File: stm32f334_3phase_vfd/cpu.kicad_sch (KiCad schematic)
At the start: 16 parts, among them J101 Conn_01x01, J102 Conn_01x01, J103 Conn_01x01, J104 Conn_01x01, U101 STM32F334K6Tx, Y101 Crystal_Small

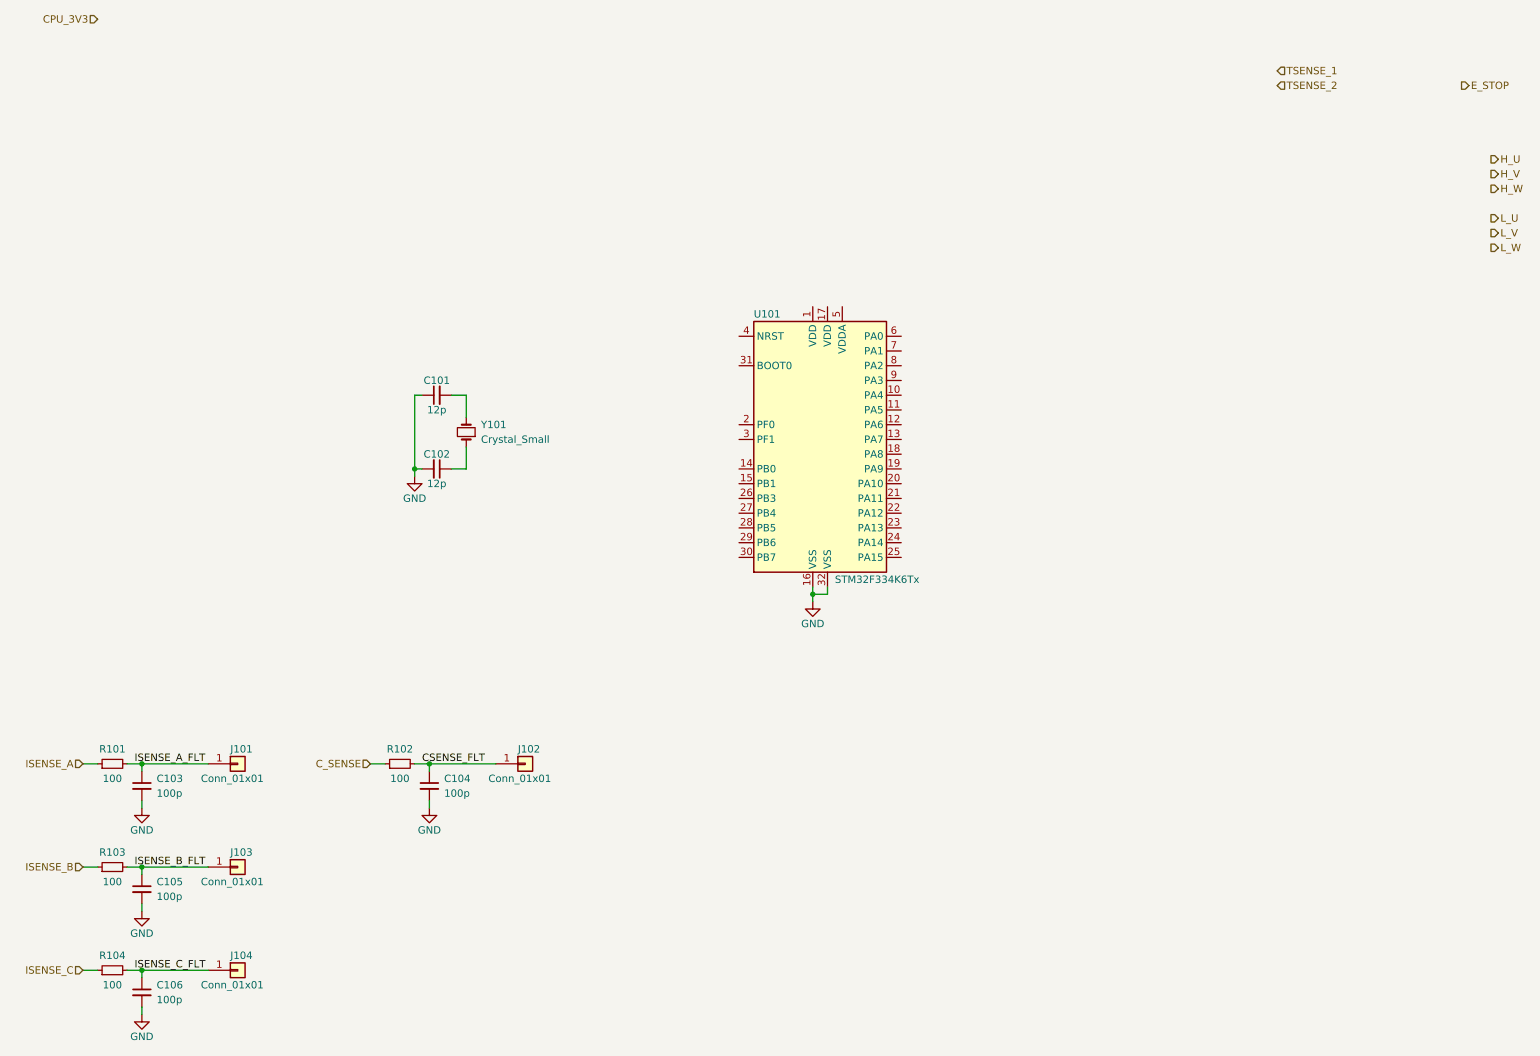
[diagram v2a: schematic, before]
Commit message: switch to LQFP48 cpu, continue workin on layout
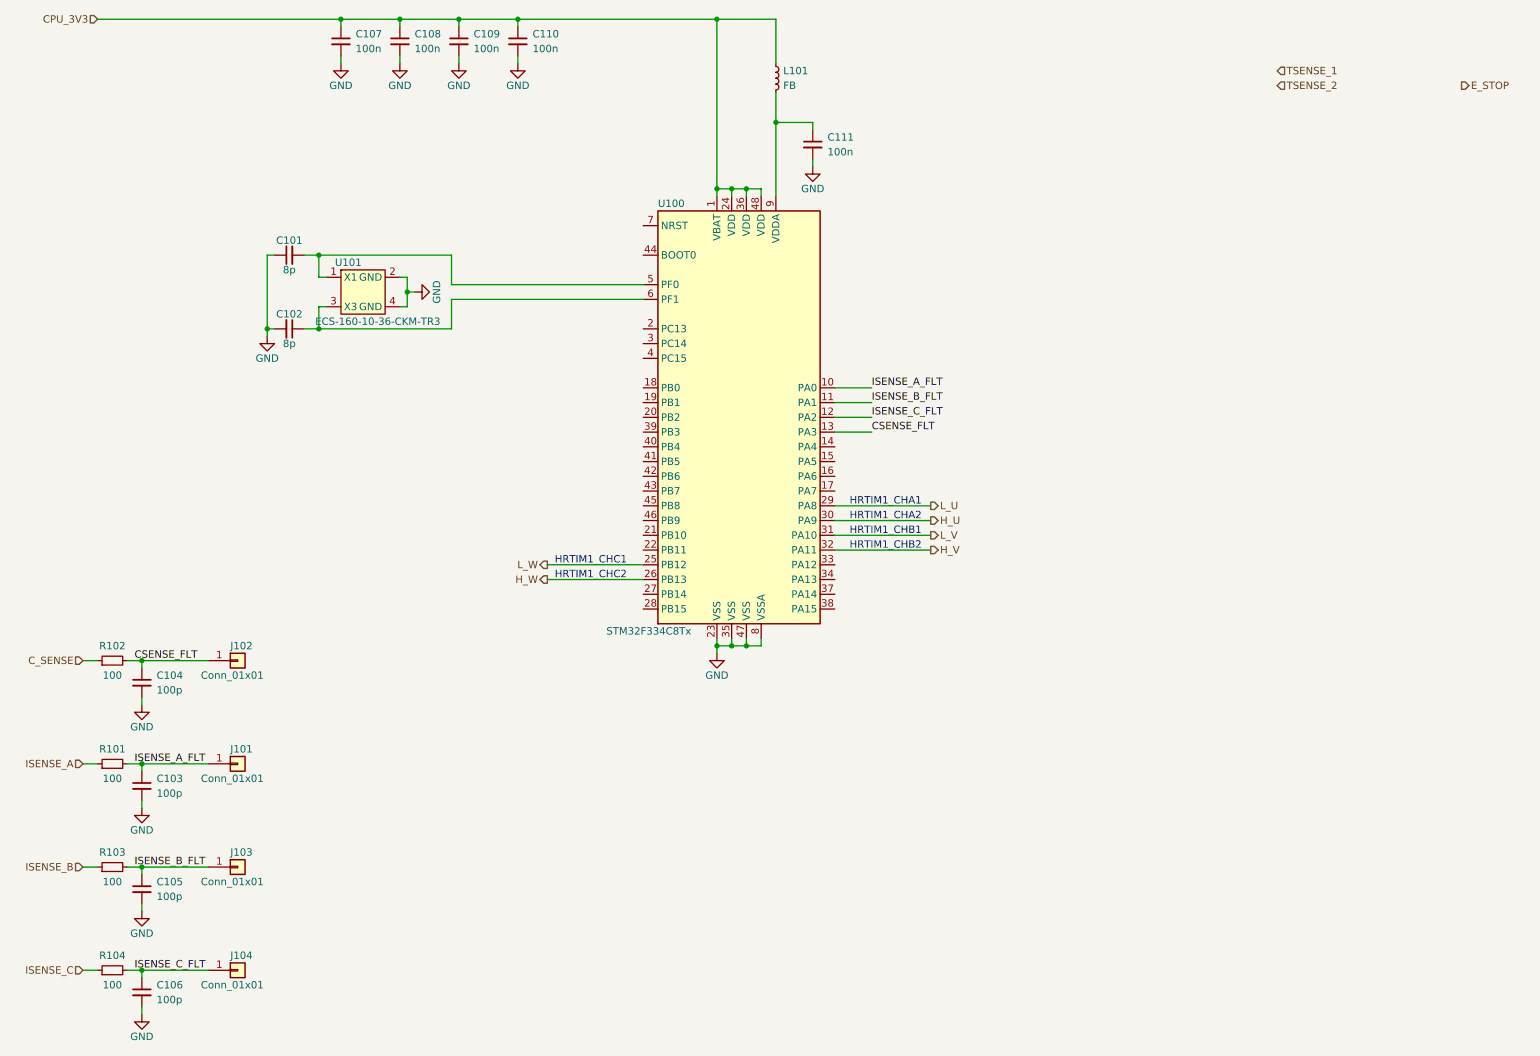
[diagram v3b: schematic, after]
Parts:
- removed U101: STM32F334K6Tx, Package_QFP:LQFP-32_7x7mm_P0.8mm, symbol MCU_ST_STM32F3:STM32F334K6Tx
- removed Y101: Crystal_Small, symbol Device:Crystal_Small
- added C107, C108, C109, C110, C111: 100n, Capacitor_SMD:C_0805_2012Metric, symbol Device:C_Small
- added L101: FB, Inductor_SMD:L_0805_2012Metric, symbol Device:L_Small
- added U100: STM32F334C8Tx, Package_QFP:LQFP-48_7x7mm_P0.5mm, symbol MCU_ST_STM32F3:STM32F334C8Tx
- added U101: ECS-160-10-36-CKM-TR3, Crystal:Crystal_SMD_2520-4Pin_2.5x2.0mm, symbol custom_parts:ECS-160-10-36-CKM-TR3
- C101, C102: value 12p -> 8p; footprint (none) -> Capacitor_SMD:C_0805_2012Metric
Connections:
- net CPU_3V3: now also C107.1, C108.1, C109.1, C110.1, L101.1, U100.1 (VBAT), U100.24 (VDD), U100.36 (VDD), U100.48 (VDD)
- net CSENSE_FLT: now also U100.13 (PA3)
- net GND: now also C107.2, C108.2, C109.2, C110.2, C111.2, U100.23 (VSS), U100.35 (VSS), U100.47 (VSS), U100.8 (VSSA), U101.2 (GND), U101.4 (GND)
- net H_U: now also U100.30 (PA9)
- net H_V: now also U100.32 (PA11)
- net H_W: now also U100.26 (PB13)
- net ISENSE_A_FLT: now also U100.10 (PA0)
- net ISENSE_B_FLT: now also U100.11 (PA1)
- net ISENSE_C_FLT: now also U100.12 (PA2)
- net L_U: now also U100.29 (PA8)
- net L_V: now also U100.31 (PA10)
- net L_W: now also U100.25 (PB12)
- net at C102.1: now also U100.6 (PF1), U101.3 (X3)
- net at C101.2: now also U100.5 (PF0), U101.1 (X1)
- new net: C111.1, L101.2, U100.9 (VDDA)
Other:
- note added: "HRTIM1_CHA1"
- note added: "HRTIM1_CHA2"
- note added: "HRTIM1_CHB1"
- note added: "HRTIM1_CHB2"
- note added: "HRTIM1_CHC1"
- note added: "HRTIM1_CHC2"
- moved on the sheet: C101, C102, C104, J102, R102
